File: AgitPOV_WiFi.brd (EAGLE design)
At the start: 41.5 x 67.6 mm, 43 parts

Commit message: Post-coffee commit
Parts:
- moved JST 5.07 mm to (6.24, 3.65), turned to 180 degrees
- moved BATT 2.29 mm to (2.86, 4.76), turned to 270 degrees
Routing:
- net GND: track 340.4 -> 354.9 mm
- net ENTREEGND: track 28.0 -> 23.6 mm
- net 5V: track 288.4 -> 284.6 mm

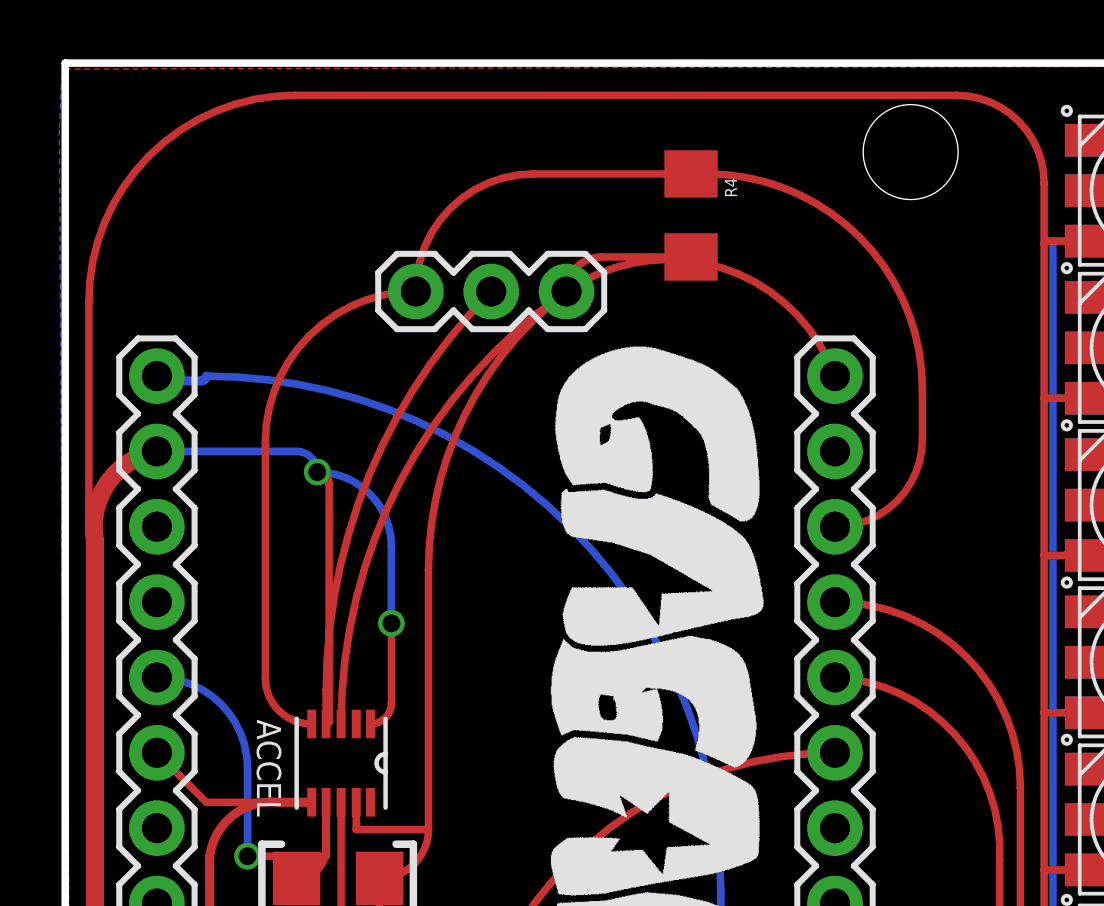
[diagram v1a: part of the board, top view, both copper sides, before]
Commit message: Sin interrupt para el ACCEL! De regresar al sensor Hall en D4.
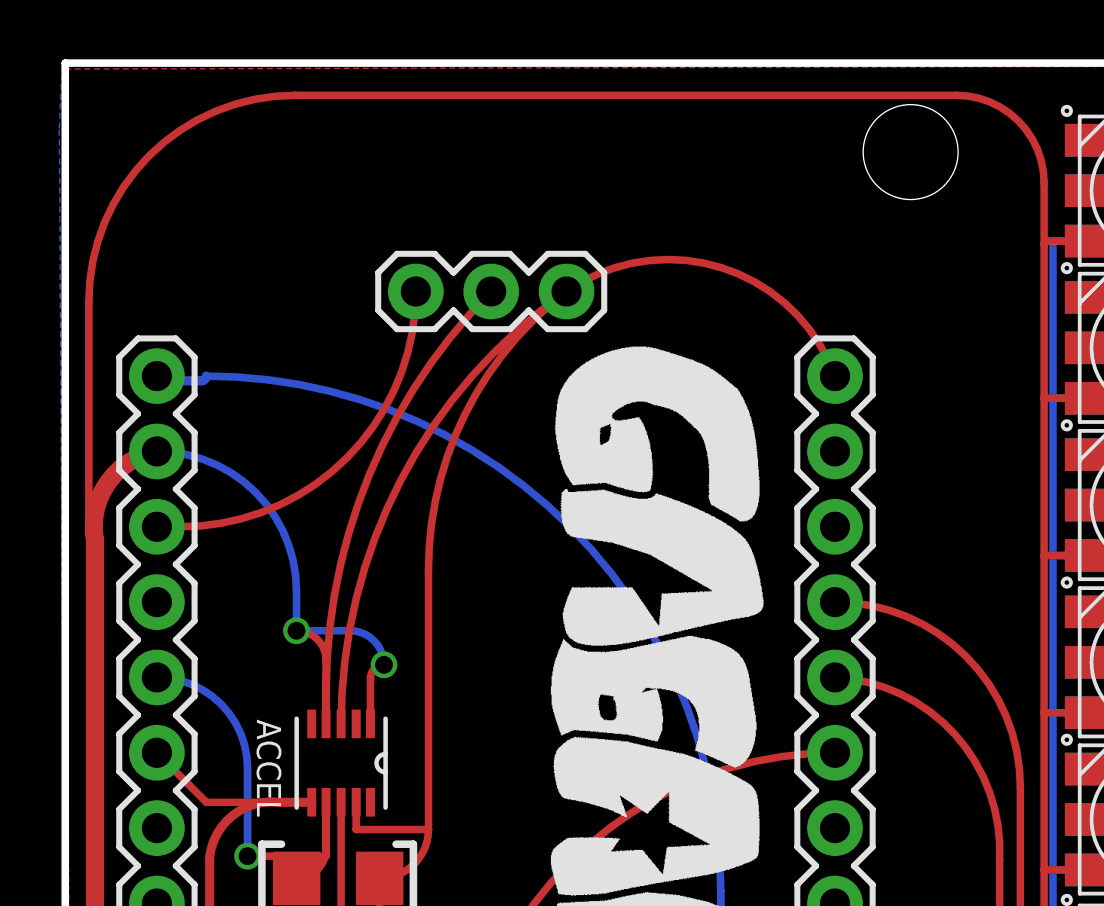
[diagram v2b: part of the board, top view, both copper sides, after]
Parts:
- removed R4: 10k, SparkFun-Resistors:1206
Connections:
- removed net INT: ACCEL.5, HALL.3, R4.1, WEMOS1.6
- new net N$41: HALL.3, WEMOS2.3
- new net N$65: WEMOS1.6
- net +3.3V: no longer R4.2
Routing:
- net INT: track 44.9 -> 0.00 mm
- net N$41: track 0.00 -> 12.0 mm
- net GND: track 354.9 -> 347.8 mm
- net +3.3V: track 68.6 -> 63.9 mm
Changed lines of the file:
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@@
 <attribute name="VALUE" x="5.4214" y="31.7484" size="0.8128" layer="27" rot="SR270"/>
-</element>
-<element name="R4" library="SparkFun-Resistors" package="1206" value="10k" x="21.45" y="62.7" smashed="yes" rot="R270">
-<attribute name="NAME" x="22.593" y="63.97" size="0.4064" layer="25" rot="R270"/>
-<attribute name="VALUE" x="19.926" y="64.097" size="0.4064" layer="27" rot="R270"/>
 </element>
 </elements>
@@
 <wire x1="1.15" y1="59.8" x2="1.15" y2="51.95904375" width="0.254" layer="1"/>
 <wire x1="1.15" y1="51.95904375" x2="1.35408125" y2="51.7549625" width="0.254" layer="1" curve="90"/>
-<wire x1="9.14608125" y1="45.5577625" x2="9.1577625" y2="45.5577625" width="0.254" layer="1"/>
-<wire x1="9.1577625" y1="45.5577625" x2="9.25" y2="45.65" width="0.254" layer="1" curve="90"/>
-<wire x1="9.25" y1="45.65" x2="9.25" y2="53.65" width="0.254" layer="1"/>
-<wire x1="9.25" y1="53.65" x2="8.85" y2="54.05" width="0.254" layer="1" curve="90"/>
-<via x="8.85" y="54.05" extent="1-16" drill="0.6" shape="square"/>
-<wire x1="8.85" y1="54.05" x2="8.1550375" y2="54.7449625" width="0.254" layer="16" curve="90"/>
-<wire x1="8.1550375" y1="54.7449625" x2="3.44408125" y2="54.7449625" width="0.254" layer="16"/>
-<wire x1="10.64468125" y1="45.5577625" x2="11.35" y2="46.26308125" width="0.254" layer="1" curve="90"/>
-<wire x1="11.35" y1="46.26308125" x2="11.35" y2="48.95" width="0.254" layer="1"/>
-<via x="11.35" y="48.95" extent="1-16" drill="0.6" shape="square"/>
-<wire x1="11.35" y1="48.95" x2="11.35" y2="51.55" width="0.254" layer="16"/>
-<wire x1="11.35" y1="51.55" x2="8.85" y2="54.05" width="0.254" layer="16" curve="90"/>
-<wire x1="35.05408125" y1="8.3369625" x2="39.05408125" y2="8.6369625" width="0" layer="19" extent="1-16"/>
+<wire x1="9.14608125" y1="45.5577625" x2="9.14608125" y2="47.70391875" width="0.254" layer="1"/>
+<wire x1="9.14608125" y1="47.70391875" x2="8.15" y2="48.7" width="0.254" layer="1" curve="90"/>
+<via x="8.15" y="48.7" extent="1-16" drill="0.6" shape="square"/>
+<wire x1="8.15" y1="48.7" x2="8.15" y2="50.03904375" width="0.254" layer="16"/>
+<wire x1="8.15" y1="50.03904375" x2="3.44408125" y2="54.7449625" width="0.254" layer="16" curve="90"/>
+<wire x1="10.64468125" y1="45.5577625" x2="10.64468125" y2="47.09468125" width="0.254" layer="1"/>
+<wire x1="10.64468125" y1="47.09468125" x2="11.1" y2="47.55" width="0.254" layer="1" curve="-90"/>
+<via x="11.1" y="47.55" extent="1-16" drill="0.6" shape="square"/>
+<wire x1="11.1" y1="47.55" x2="9.95" y2="48.7" width="0.254" layer="16" curve="90"/>
+<wire x1="9.95" y1="48.7" x2="8.15" y2="48.7" width="0.254" layer="16"/>
 </signal>
 <signal name="+3.3V">
@@
 <wire x1="12.6" y1="41.99888125" x2="10.16208125" y2="41.99888125" width="0.254" layer="1"/>
 <wire x1="10.16208125" y1="41.99888125" x2="10.16208125" y2="42.9161625" width="0.254" layer="1"/>
-<contactref element="R4" pad="2"/>
-<wire x1="21.45" y1="61.3" x2="18.41711875" y2="61.3" width="0.254" layer="1"/>
-<wire x1="18.41711875" y1="61.3" x2="17.25408125" y2="60.1369625" width="0.254" layer="1" curve="90"/>
 </signal>
 <signal name="N$6">
@@
 <wire x1="6.5" y1="44.06904375" x2="3.44408125" y2="47.1249625" width="0.254" layer="16" curve="90"/>
 </signal>
-<signal name="INT">
-<contactref element="ACCEL" pad="5"/>
-<contactref element="HALL" pad="3"/>
-<contactref element="R4" pad="1"/>
-<wire x1="21.45" y1="64.1" x2="16.13711875" y2="64.1" width="0.254" layer="1"/>
-<wire x1="16.13711875" y1="64.1" x2="12.17408125" y2="60.1369625" width="0.254" layer="1" curve="90"/>
-<wire x1="8.66348125" y1="45.5577625" x2="8.6422375" y2="45.5577625" width="0.254" layer="1"/>
-<wire x1="8.6422375" y1="45.5577625" x2="7.1" y2="47.1" width="0.254" layer="1" curve="-90"/>
-<wire x1="7.1" y1="47.1" x2="7.1" y2="55.06288125" width="0.254" layer="1"/>
-<wire x1="7.1" y1="55.06288125" x2="12.17408125" y2="60.1369625" width="0.254" layer="1" curve="-90"/>
-<contactref element="WEMOS1" pad="6"/>
-<wire x1="26.30408125" y1="52.2049625" x2="29.25" y2="55.15088125" width="0.254" layer="1" curve="90"/>
-<wire x1="29.25" y1="55.15088125" x2="29.25" y2="56.85" width="0.254" layer="1"/>
-<wire x1="29.25" y1="56.85" x2="22" y2="64.1" width="0.254" layer="1" curve="90"/>
-<wire x1="22" y1="64.1" x2="21.45" y2="64.1" width="0.254" layer="1"/>
-</signal>
 <signal name="PULLDOWN">
 <contactref element="PUSHBUTTON" pad="3"/>
@@
 <signal name="N$5">
 </signal>
+<signal name="N$41">
+<contactref element="HALL" pad="3"/>
+<contactref element="WEMOS2" pad="3"/>
+<wire x1="12.17408125" y1="60.1369625" x2="4.24208125" y2="52.2049625" width="0.254" layer="1" curve="-90"/>
+<wire x1="4.24208125" y1="52.2049625" x2="3.44408125" y2="52.2049625" width="0.254" layer="1"/>
+</signal>
+<signal name="N$65">
+<contactref element="WEMOS1" pad="6"/>
+</signal>
 </signals>

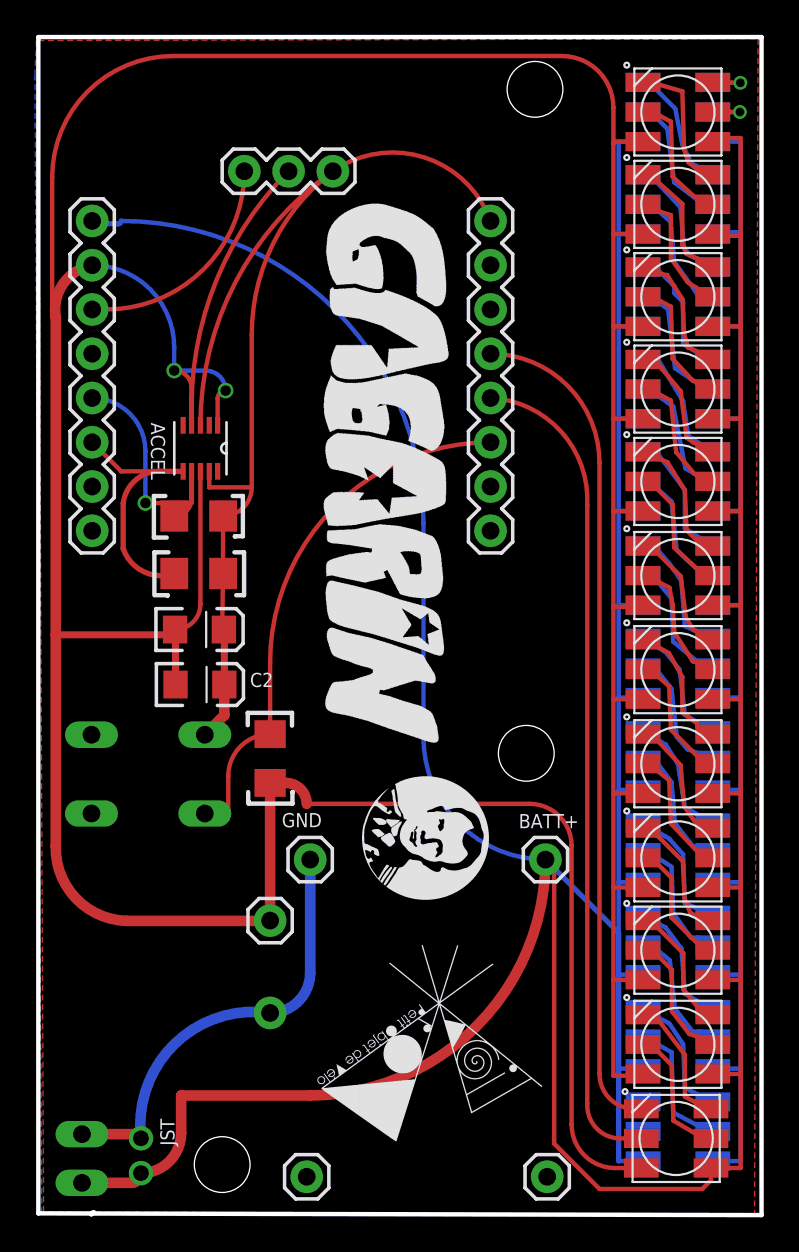
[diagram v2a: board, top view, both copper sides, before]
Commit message: Swapped the MMA7660 for the MMA8452Q
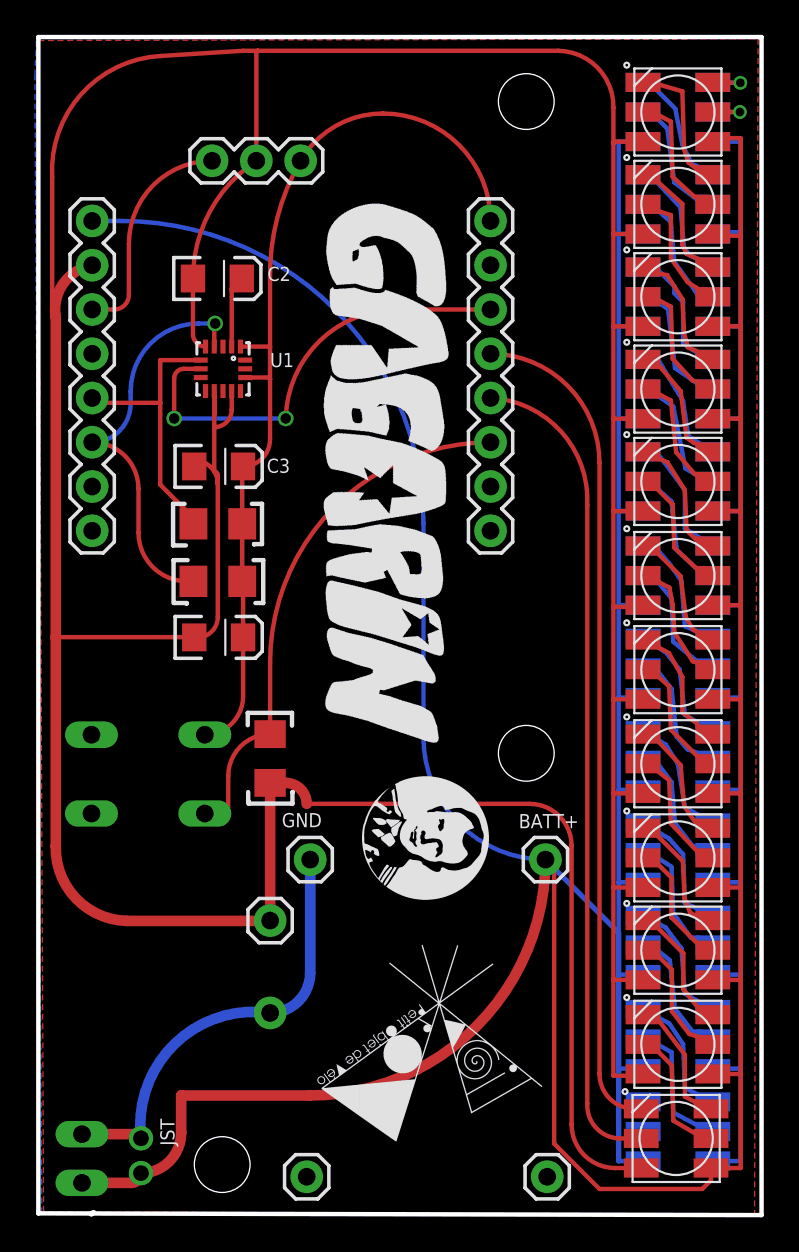
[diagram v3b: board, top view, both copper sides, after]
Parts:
- removed ACCEL: MMA7660FCT, Freescale_By_element14_Batch_1:DFN300X300X100-10N
- added C3: 4.7uF, SparkFun-Capacitors:EIA3216
- added U1: MMA8452Q, SparkFun-Sensors:QFN-16_0.5MM
- moved C2 23.3 mm to (10.6, 54.0)
- moved HALL 1.94 mm to (15.4, 60.7)
- moved R2 1.19 mm to (10.7, 36.6)
- moved C1 1.19 mm to (10.7, 33.4)
- moved R1 1.19 mm to (10.7, 39.9)
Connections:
- removed net N$65: WEMOS1.6
- new net BYP: C2.A, U1.2
- new net SA0: U1.7, WEMOS1.6
- net +3.3V: now also C3.A, U1.1, U1.14; no longer ACCEL.3, ACCEL.9, C2.A
- net GND: now also C3.C, U1.10, U1.12, U1.5; no longer ACCEL.1, ACCEL.4, ACCEL.8
- net SCL: now also U1.4; no longer ACCEL.6
- net SDA: now also U1.6; no longer ACCEL.7
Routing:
- net SA0: track 0.00 -> 24.7 mm, vias 0 -> 2
- net +3.3V: track 63.9 -> 52.1 mm
- net SCL: track 15.8 -> 22.2 mm, vias 0 -> 1
- net GND: track 347.8 -> 341.8 mm, vias 2 -> 0
- net BYP: track 0.00 -> 4.15 mm
- net SDA: track 14.7 -> 16.5 mm, vias 1 -> 0

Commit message: Added pin headers for INT1 and INT2
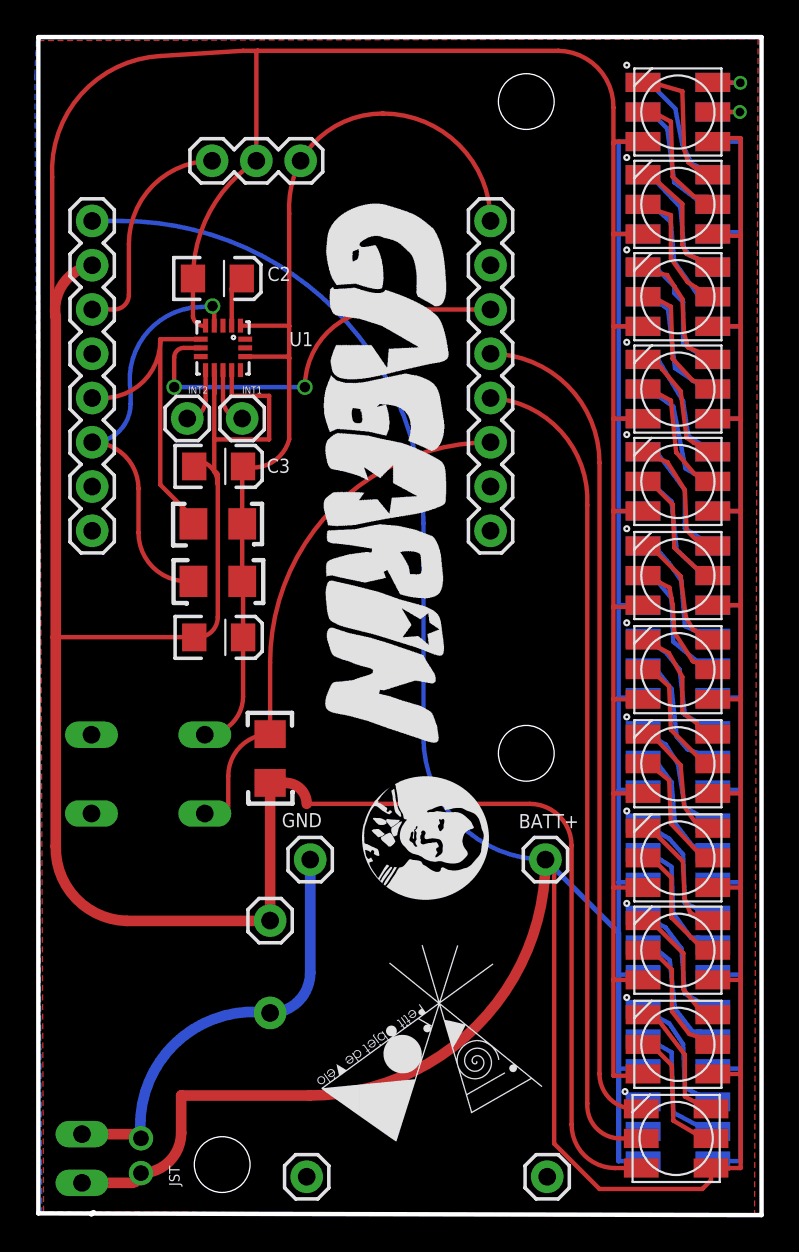
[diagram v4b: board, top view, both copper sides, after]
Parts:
- added INT1, INT2: (no value), SparkFun-Connectors:1X01
- moved U1 1.20 mm to (10.9, 50.0)
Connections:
- new net N$65: INT1.1, U1.11
- new net N$67: INT2.1, U1.9
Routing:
- net GND: track 341.8 -> 348.7 mm
- net N$65: track 0.00 -> 3.23 mm
- net N$67: track 0.00 -> 3.21 mm
- net +3.3V: track 52.1 -> 55.0 mm
- net SDA: track 16.5 -> 19.0 mm
- net SA0: track 24.7 -> 23.5 mm
- net BYP: track 4.15 -> 2.95 mm
- net SCL: track 22.2 -> 22.8 mm
